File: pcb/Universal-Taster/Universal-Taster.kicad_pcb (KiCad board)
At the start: 2 copper layers, 30 x 30 mm, 59 parts, among them J1 I2C, J2 INTERFACE, J3 Val**, J4 JTAG, SW1 PROG, U1 EFM32PG12B500, U2 NCN5121, U3 MX25R8035F, Y1 32.768kHz, Y2 40MHz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

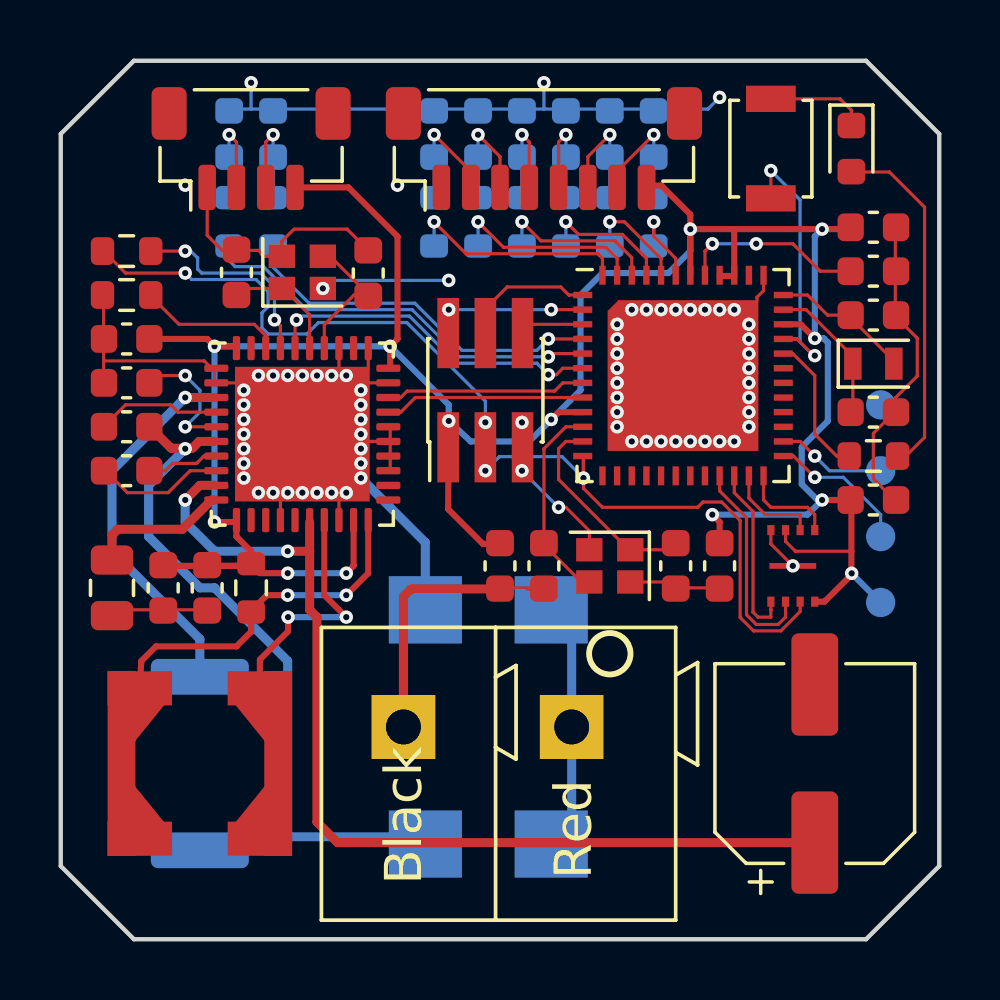
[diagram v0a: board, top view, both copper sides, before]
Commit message: Fix universal taster
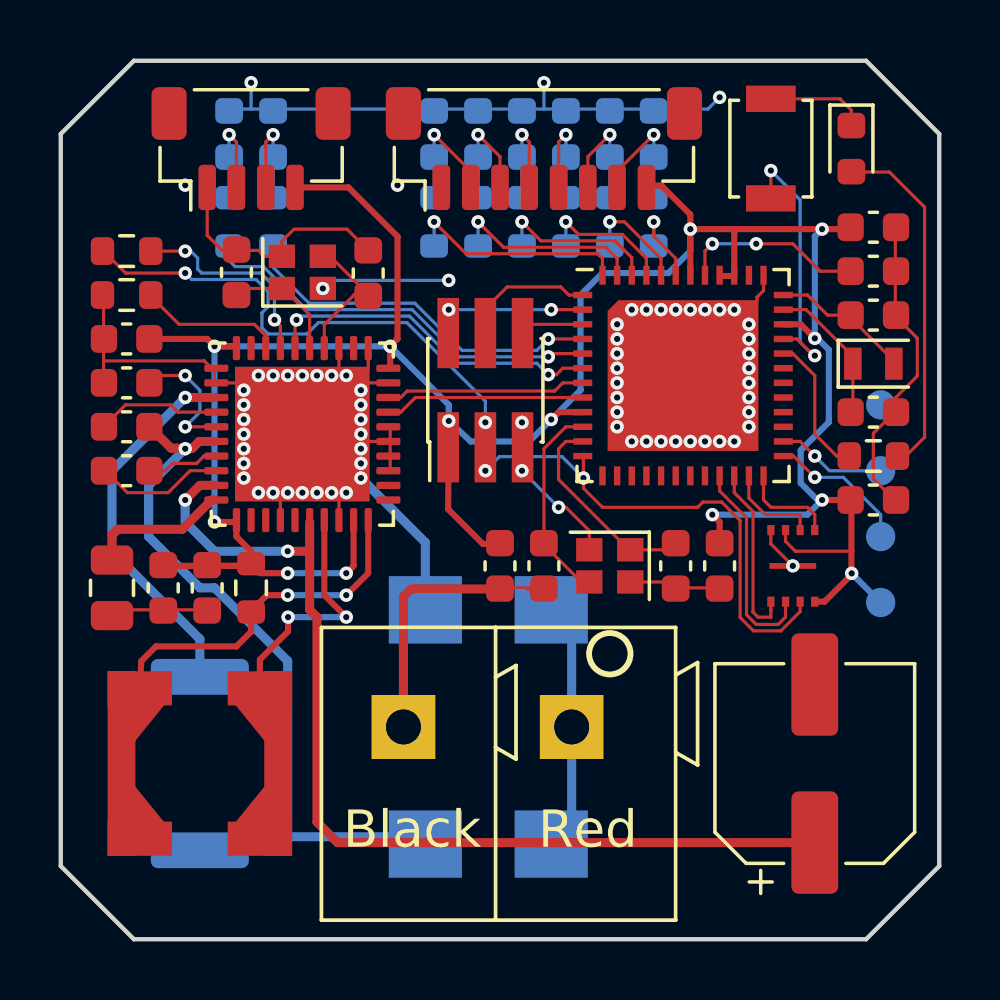
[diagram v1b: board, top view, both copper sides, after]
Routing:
- net /SWITCH: track 9.75 -> 9.22 mm
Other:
- board text added: "BasilFX 10/2022 V1.3.1"
- board text removed: "BasilFX 09/2022 V1.3.0"

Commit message: Add interactive BoM to Universal Taster
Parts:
- J3: value Val** -> KNX_KLEMME
